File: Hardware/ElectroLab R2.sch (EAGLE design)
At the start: 226 parts, among them IC1 LM2902DT, IC10 CD4511BNSR, IC11 PAM8403, IC2 LM2902DT, IC3 SN74LV08ADR, IC4 SN74LV32ADR, IC5 SN74LV04ADR, IC6 4027D, IC7 4027D, IC8 NE555D, IC9 AT42QT1012, P1 SLIDE_POT_20MM, P2 ALPS_RK09K_VERTICAL, P3 ALPS_RK09K_VERTICAL, U1 USB, U2 USB-B

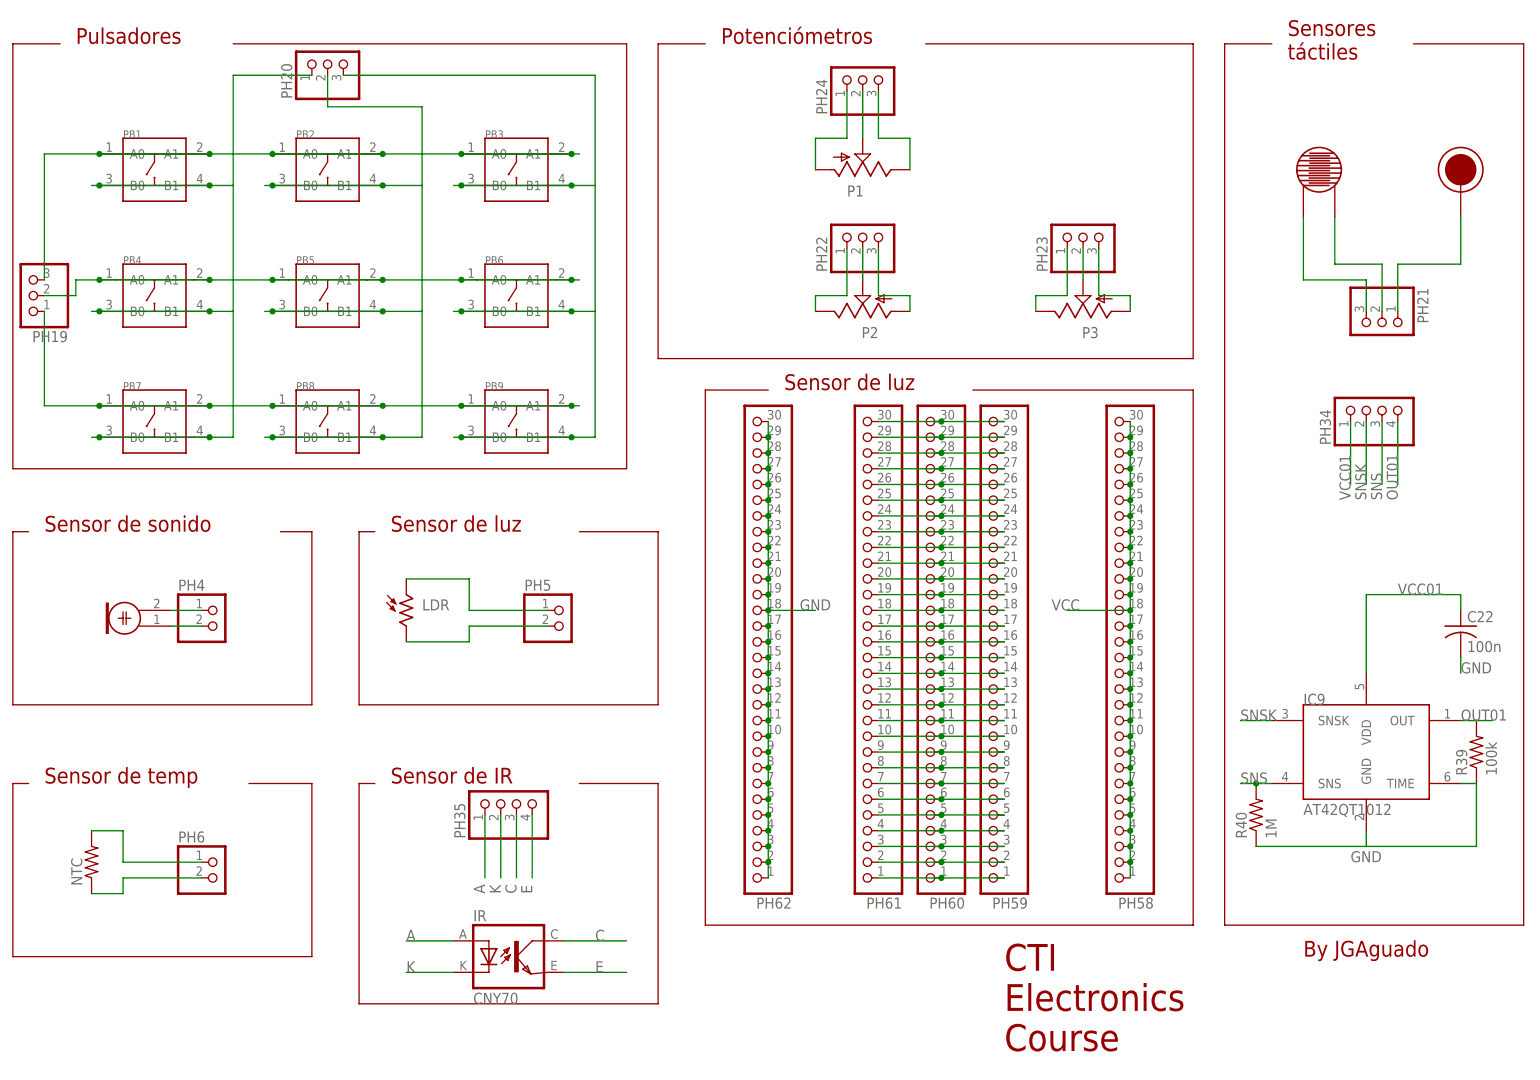
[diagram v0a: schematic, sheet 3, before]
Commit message: IR sensor replaced with ADXL337 analog accelerometer. 5v to 3.3V power supply IC integrated. Analog level shift circuit based on Op. Amps 3.3v to 5V.
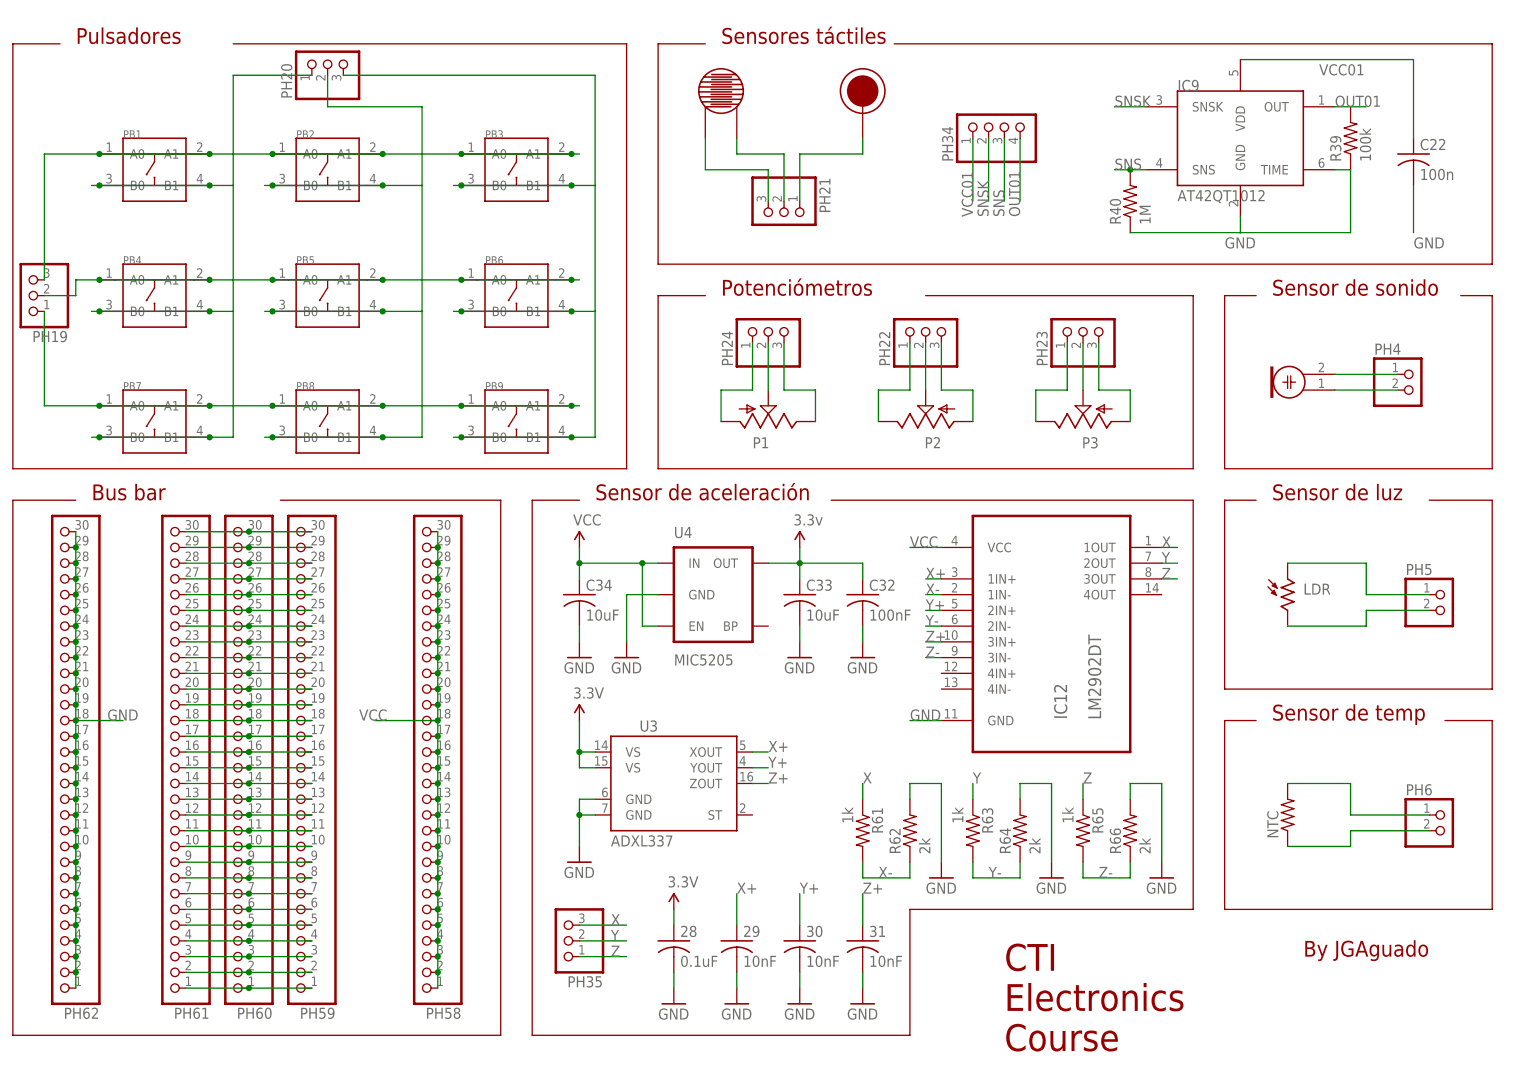
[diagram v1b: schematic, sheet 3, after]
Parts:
- removed IR: CNY70, cny70:CNY70
- added 28: 0.1uF, resistor:C-USC1206
- added 29, 30, 31: 10nF, resistor:C-USC1206
- added C32: 100nF, resistor:C-USC1206
- added C33, C34: 10uF, resistor:C-USC1206
- added IC12: LM2902DT, Texas Instruments_By_element14_Batch_1:LM2902DT
- added R61, R63, R65: 1k, resistor:R-US_R1206
- added R62, R64, R66: 2k, resistor:R-US_R1206
- added U3: ADXL337, SparkFun-Sensors:ADXL337
- added U4: MIC5205, SparkFun:V_REG_LDOSMD
- PH35: device pinhead:PINHD-1X4 -> pinhead:PINHD-1X3
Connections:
- removed net A: IR.A, PH35.1
- removed net C: IR.COL, PH35.3
- removed net E: IR.EMI, PH35.4
- removed net K: IR.C, PH35.2
- new net 3.3V: 28.1, C32.1, C33.1, U3.VS@1, U3.VS@2, U4.OUT
- new net X: IC12.1OUT, PH35.3, R61.1
- new net X+: 29.1, IC12.1IN+, U3.XOUT
- new net X-: IC12.1IN-, R61.2, R62.1
- new net Y: IC12.2OUT, PH35.2, R63.1
- new net Y+: 30.1, IC12.2IN+, U3.YOUT
- new net Y-: IC12.2IN-, R63.2, R64.1
- new net Z: IC12.3OUT, PH35.1, R65.1
- new net Z+: 31.1, IC12.3IN+, U3.ZOUT
- new net Z-: IC12.3IN-, R65.2, R66.1
- net GND: now also 28.2, 29.2, 30.2, 31.2, C32.2, C33.2, C34.2, IC12.GND, R62.2, R64.2, R66.2, U3.GND@1, U3.GND@2, U4.GND
- net VCC: now also C34.1, IC12.VCC, U4.EN, U4.IN
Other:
- note added: "Bus bar"
- note added: "Sensor de aceleración"
- note removed: "Sensor de IR"
- moved on the sheet: C22, IC9, LDR, NTC, P1, P2, P3, PH21, PH22, PH23, PH24, PH34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

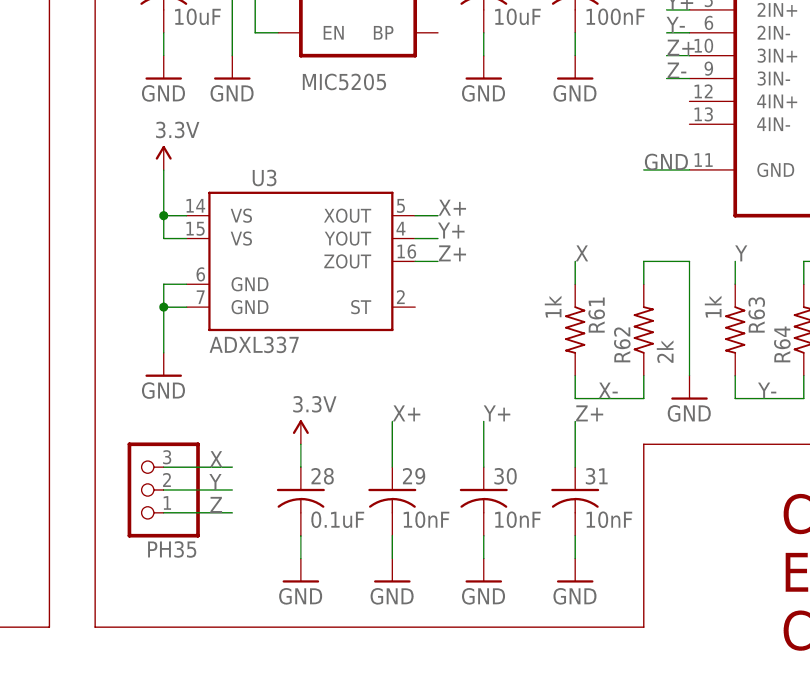
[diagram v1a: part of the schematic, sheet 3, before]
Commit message: Analogic accelerometer ADXL337 Layout in BRD
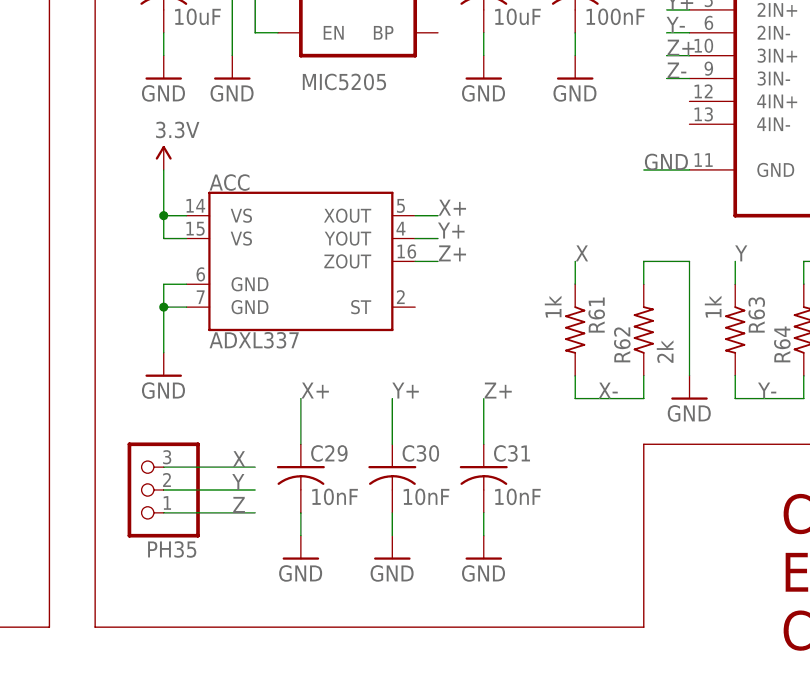
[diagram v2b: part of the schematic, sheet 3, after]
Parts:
- removed 28: 0.1uF, resistor:C-USC1206
- removed 29, 30, 31: 10nF, resistor:C-USC1206
- removed U3: ADXL337, SparkFun-Sensors:ADXL337
- added ACC: ADXL337, SpaceDIY_IC:ADXL337
- added C29, C30, C31: 10nF, SpaceDIY_passive_components:C0603
- C32, C33, C34: device resistor:C-USC1206 -> SpaceDIY_passive_components:C0603
- R61, R62, R63, R64, R65, R66: device resistor:R-US_R1206 -> SpaceDIY_passive_components:R0603
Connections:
- net 3.3V: now also ACC.VS@1, ACC.VS@2; no longer 28.1, U3.VS@1, U3.VS@2
- net GND: now also ACC.GND@1, ACC.GND@2, C29.2, C30.2, C31.2; no longer 28.2, 29.2, 30.2, 31.2, U3.GND@1, U3.GND@2
- net X+: now also ACC.XOUT, C29.1; no longer 29.1, U3.XOUT
- net Y+: now also ACC.YOUT, C30.1; no longer 30.1, U3.YOUT
- net Z+: now also ACC.ZOUT, C31.1; no longer 31.1, U3.ZOUT

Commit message: Modified capacitive tactile sensor. Simplified design.
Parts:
- removed PH34: (no value), pinhead:PINHD-1X4
- added C28: 10nF, SpaceDIY_passive_components:C0603
- added R67: 10k, SpaceDIY_passive_components:R0603
- C22: device resistor:C-USC1206 -> SpaceDIY_passive_components:C0603
- R39, R40: device resistor:R-US_R1206 -> SpaceDIY_passive_components:R0603
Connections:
- removed net N$252: PH21.2, U$16.0
- removed net N$253: PH21.1, U$15.0
- removed net VCC01: C22.1, IC9.VDD, PH34.1
- new net N$125: PH21.1, U$16.0
- new net SENSE: R67.1, U$15.0
- net OUT01: now also PH21.2; no longer PH34.4
- net SNS: now also C28.2; no longer PH34.3
- net SNSK: now also C28.1, R67.2; no longer PH34.2
- net VCC: now also C22.1, IC9.VDD
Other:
- moved on the sheet: C22, IC9, R39, R40

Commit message: Upgraded Electrolitic Capacitors to Tantalum Capacitors (C15-C18, C27)
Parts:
- C17, C18: device resistor:CPOL-US153CLV-0605 -> rcl:CPOL-USA/3216-18W
- C19, C20: device resistor:CPOL-US153CLV-0810 -> rcl:CPOL-USD/7343-31W
- C27: device resistor:CPOL-US153CLV-0605 -> rcl:CPOL-USD/7343-31W

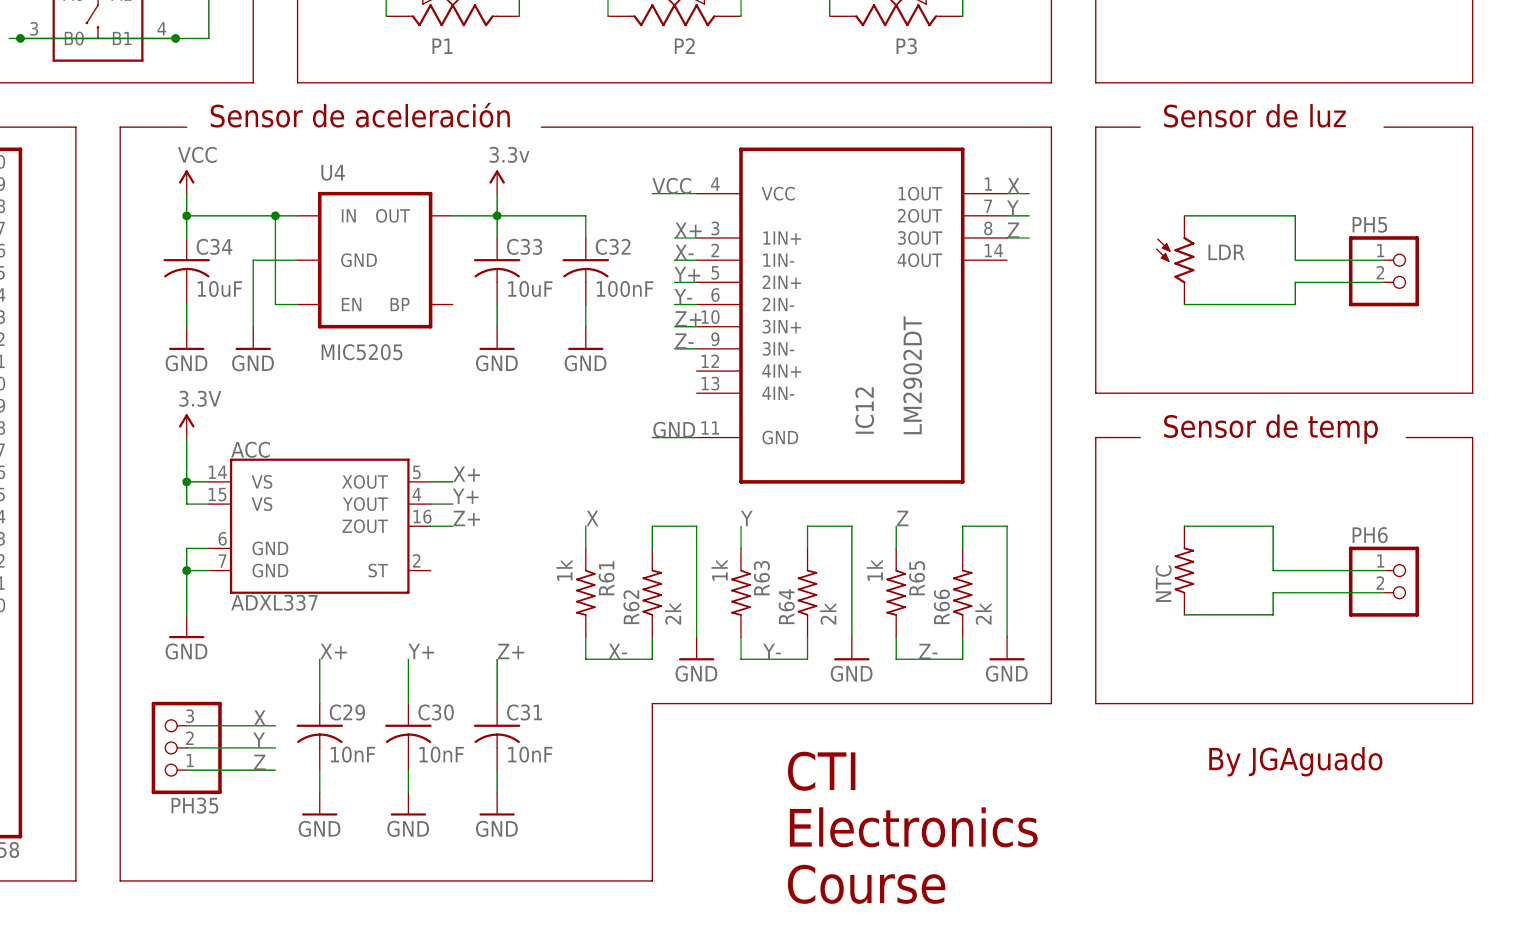
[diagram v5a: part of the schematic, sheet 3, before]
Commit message: Jumpers added to accelerometer outputs to optionally get the raw signal
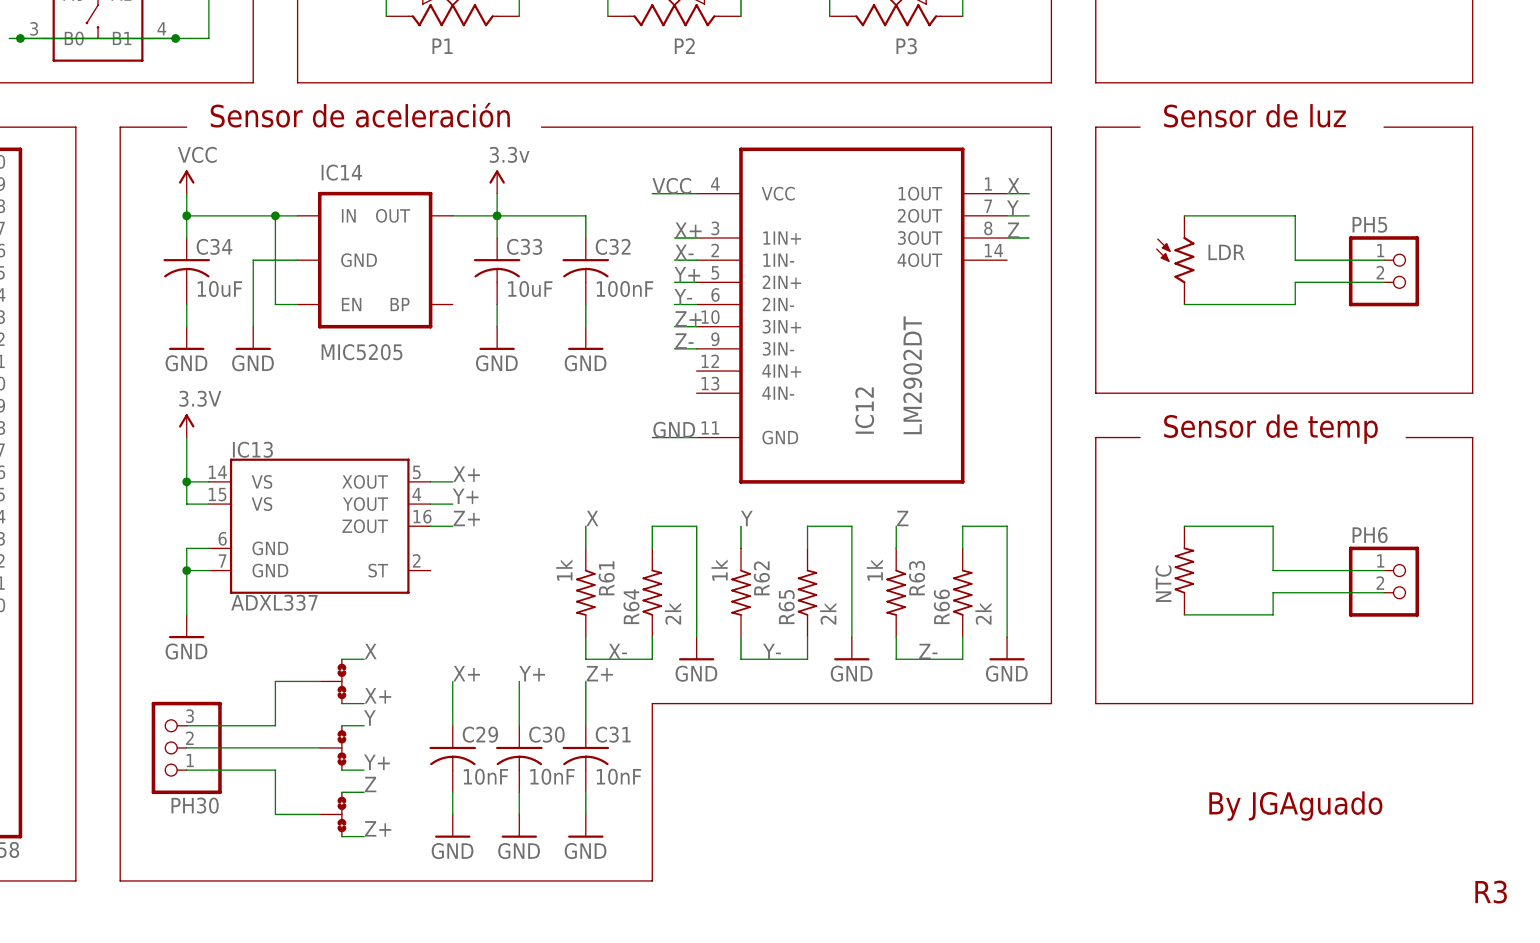
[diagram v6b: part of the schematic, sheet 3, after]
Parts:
- added JMP7, JMP8, JMP9: 0R-JUMPA, jump-0r-smd:0R-JUMPA
- PH30: device pinhead:PINHD-1X4 -> pinhead:PINHD-1X3
- PH35: device pinhead:PINHD-1X3 -> pinhead:PINHD-1X4
- R62: value 2k -> 1k
- R65: value 1k -> 2k
- renumbered ACC to IC13, SV1 to PH63, U4 to IC14
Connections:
- new net N$124: JMP8-0R.2, PH30.2
- new net N$127: JMP7-0R.2, PH30.3
- new net N$128: JMP9-0R.2, PH30.1
- net GND: now also R65.2; no longer R62.2
- net IA: now also PH35.1; no longer PH30.1
- net IB: now also PH35.2; no longer PH30.2
- net IC: now also PH35.3; no longer PH30.3
- net ID: now also PH35.4; no longer PH30.4
- net X: now also JMP7-0R.3; no longer PH35.3
- net X+: now also JMP7-0R.1
- net X-: now also R64.1; no longer R62.1
- net Y: now also JMP8-0R.3, R62.1; no longer PH35.2, R63.1
- net Y+: now also JMP8-0R.1
- net Y-: now also R62.2, R65.1; no longer R63.2, R64.1
- net Z: now also JMP9-0R.3, R63.1; no longer PH35.1, R65.1
- net Z+: now also JMP9-0R.1
- net Z-: now also R63.2; no longer R65.2
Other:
- note added: "R3"
- note removed: "CTI Electronics Course"
- moved on the sheet: C29, C30, C31, R62, R63, R64, R65
